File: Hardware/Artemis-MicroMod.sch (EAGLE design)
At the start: 24 parts, among them J2 MICROMOD-2222, U1 ARTEMIS_MODULESMD, U6 CH340E_MSOP10, Y1 32.768kHz

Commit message: Adding panel files for v10
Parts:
- removed J2: MICROMOD-2222, Teensy:MICROMOD-2222
- added C1: 0.1uF, SparkFun-Capacitors:0.1UF-0402T-16V-10%
- added J1: MICROMOD-2222, SparkFun-MicroMod:MICROMOD-2222
- added R2, R3, R6: 100k, SparkFun-Resistors:100KOHM-0402T-1/16W-1%
- added R4, R5, R7: 150k, SparkFun-Resistors:150KOHM-0402T-1/16W-1%
- added U2: TSV524, OpAmp:TSV524
- C17: device SparkFun-Capacitors:10NF-0603-50V-10% -> SparkFun-Capacitors:10NF-0402T-25V-10%
- C18: device SparkFun-Capacitors:0.1UF-0603-25V-(+80/-20%) -> SparkFun-Capacitors:0.1UF-0402T-16V-10%
- C20, C21: device SparkFun-Capacitors:0.1UF-0603-25V-5% -> SparkFun-Capacitors:0.1UF-0402T-16V-10%
- C28: value 1nF -> 1.0nF; device SparkFun-Capacitors:1.0NF/1000PF-0603-50V-10% -> SparkFun-Capacitors:1.0NF/1000PF-0402_TIGHT-50V-10%
- R14: device SparkFun-Resistors:100KOHM-0603-1/10W-1% -> SparkFun-Resistors:100KOHM-0402T-1/16W-1%
- R15: value 220k -> 220KOHM-0402T-1/16W-1%; device SparkFun-Resistors:220KOHM-0603-1/10W-1% -> SparkFun-Resistors:220KOHM-0402T-1/16W-1%
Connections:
- removed net GPIO11: J2.G11, U1.~AD11(PDMDATA)
- removed net GPIO8: J2.G8, U1.(SLNCE/I2SWCLK)D3
- removed net N$8: C13.2, U1.XI, Y1.1
- removed net RTS0: J2.RTS1, U1.(MOSI1/TX1/PDMCLK)D10
- removed net RX0: J2.RX1, U1.(SDA2/MISO2/RX1)~D25
- removed net TX0: J2.TX1, U1.(TX1/32KHZ/SWO)~D24
- new net 3.3V_EN: J1.3.3V_EN, U1.(SLNCE/I2SWCLK)D3
- new net CAM_PCLK: J1.AUD_IN/CAM_PCLK, U1.~AD11(PDMDATA)
- new net N$10: R2.1, R4.2, U2G1.+IN
- new net N$3: R6.1, R7.2, U2G3.+IN
- new net N$4: U1.XI
- new net N$5: C13.2, Y1.1
- new net N$9: R3.1, R5.2, U2G2.+IN
- new net RTS1: J1.RTS1, U1.(MOSI1/TX1/PDMCLK)D10
- new net RX1: J1.RX1, U1.(SDA2/MISO2/RX1)~D25
- new net SCALED_ADC0: U1.~AD32(SCCIO), U2G2.-IN, U2G2.OUT
- new net SCALED_ADC1: U1.~AD35(TX1/I2SDAT/PDMCLK), U2G3.-IN, U2G3.OUT
- new net SCALED_BATT_VIN/3: U1.~AD31(SCCCLK), U2G1.-IN, U2G1.OUT
- new net TX1: J1.TX1, U1.(TX1/32KHZ/SWO)~D24
- net !RESET!: now also J1.!RESET!; no longer J2.!RESET!
- net 3.3V: now also C1.1, J1.3.3V, J1.RTC_3V, U2G5.V+; no longer J2.3.3V
- net ADC0: now also J1.A0, R3.2; no longer J2.A0, U1.~AD32(SCCIO)
- net ADC1: now also J1.A1, R6.2; no longer J2.A1, U1.~AD35(TX1/I2SDAT/PDMCLK)
- net ADC_D+: now also J1.G10/ADC_D+/CAM_VSYNC; no longer J2.G10/ADC_D+
- net ADC_D-: now also J1.G9/ADC_D-/CAM_HSYNC; no longer J2.G9/ADC_D-
- net BATT_VIN/3: now also J1.BATT_VIN/3, R2.2; no longer J2.BATT_VIN/3, U1.~AD31(SCCCLK)
- net BOOT: now also J1.!BOOT!; no longer J2.!BOOT!
- net CLKOUT: now also J1.AUD_OUT/CAM_MCLK; no longer J2.AUD_MCLK/CLKOUT
- net CTS1: now also J1.CTS1; no longer J2.CTS1
- net D0: now also J1.D0; no longer J2.D0
- net D1: now also J1.D1/CAM_TRIG; no longer J2.D1
- net GND: now also C1.2, J1.GND, R4.1, R5.1, R7.1, U2G5.V-; no longer J2.GND
- net GPIO0: now also J1.G0/BUS0; no longer J2.G0
- net GPIO1: now also J1.G1/BUS1; no longer J2.G1
- net GPIO2: now also J1.G2/BUS2; no longer J2.G2
- net GPIO3: now also J1.G3/BUS3; no longer J2.G3
- net GPIO4: now also J1.G4/BUS4; no longer J2.G4
- net GPIO5: now also J1.G5/BUS5; no longer J2.G5
- net GPIO6: now also J1.G6/BUS6; no longer J2.G6
- net GPIO7: now also J1.G7/BUS7; no longer J2.G7
- net I2C_!INT!: now also J1.I2C_!INT!; no longer J2.I2C_!INT!
- net PDM_CLK: now also J1.AUD_BCLK; no longer J2.AUD_CLK
- net PDM_DATA: now also J1.AUD_LRCLK; no longer J2.AUD_DATA
- net PWM0: now also J1.PWM0; no longer J2.PWM0
- net PWM1: now also J1.PWM1; no longer J2.PWM1
- net SCL: now also J1.I2C_SCL; no longer J2.I2C_SCL
- net SCL1: now also J1.I2C_SCL1; no longer J2.I2C_SCL1
- net SDA: now also J1.I2C_SDA; no longer J2.I2C_SDA
- net SDA1: now also J1.I2C_SDA1; no longer J2.I2C_SDA1
- net SDIO_DATA0: now also J1.SDIO_DATA0/MISO1; no longer J2.SDIO_DATA0/MISO1
- net SDIO_DATA1: now also J1.SDIO_DATA1; no longer J2.SDIO_DATA1
- net SDIO_DATA2: now also J1.SDIO_DATA2; no longer J2.SDIO_DATA2
- net SDIO_DATA3: now also J1.SDIO_DATA3; no longer J2.SDIO_DATA3
- net SPI_!CS!: now also J1.SPI_!CS!; no longer J2.SPI_!CS!
- net SPI_MISO: now also J1.SPI_MISO; no longer J2.SPI_MISO
- net SPI_MOSI: now also J1.SPI_MOSI/LED_DAT; no longer J2.LED_DAT/SPI_MOSI
- net SPI_MOSI1: now also J1.SDIO_CMD/MOSI1; no longer J2.SDIO_CMD/MOSI1
- net SPI_SCK: now also J1.SPI_SCK/LED_CLK; no longer J2.LED_CLK/SPI_SCK
- net SPI_SCK1: now also J1.SDIO_CLK/SCK1; no longer J2.SDIO_CLK/SCK1
- net SWDCK: now also J1.SWDCK; no longer J2.SWDCK
- net SWDIO: now also J1.SWDIO; no longer J2.SWDIO
- net USB_D+: now also J1.USB_D+; no longer J2.USB_D+
- net USB_D-: now also J1.USB_D-; no longer J2.USB_D-
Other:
- note added: "MicroMod Connector"

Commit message: Routed CAM_PCLK
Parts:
- removed LOGO2: SFE_LOGO_FLAME.1_INCH, SparkFun-Aesthetics:SFE_LOGO_FLAME.1_INCH
- C11, C13: device SparkFun-Capacitors:15PF-0603-50V-5% -> SparkFun-Capacitors:15PF-0402T-50V-5%
- R1: device SparkFun-Resistors:1KOHM-0603-1/10W-1% -> SparkFun-Resistors:1KOHM-0402T-1/16W-1%
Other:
- note added: "3.3V to 2V Scaling"
- moved on the sheet: C1, R2, R3, R4, R5, R6, R7, U2G1, U2G2, U2G3, U2G5

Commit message: Double buffered ADC.
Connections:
- net N$3 renamed ADC1_BUFF2
- net N$9 renamed ADC0_BUFF2
- removed net N$10: R2.1, R4.2, U2G1.+IN
- new net ADC0_BUFF1: R3.2, U2G1.-IN, U2G1.OUT
- new net ADC_BUFF1: R6.2, U2G4.-IN, U2G4.OUT
- net ADC0: now also U2G1.+IN; no longer R3.2
- net ADC1: now also U2G4.+IN; no longer R6.2
- net SCALED_BATT_VIN/3: now also R2.1, R4.2; no longer U2G1.-IN, U2G1.OUT
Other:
- moved on the sheet: C11, C13, J1, R6, R7, U1, U2G1, U2G3, Y1

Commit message: Add reverse diode to prevent RTC 3.3V from driving 3.3V bus. Add test sketches.
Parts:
- added D7: 1A/23V/620mV, SparkFun-DiscreteSemi:DIODE-SCHOTTKY-BAT20J
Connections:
- new net 3.3V_MAIN: D7.A, J1.3.3V
- net 3.3V: now also D7.C; no longer J1.3.3V

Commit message: Add MicroMod logo, double route MCLK.
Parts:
- added LOGO2: SFE_LOGO_FLAME.1_INCH, SparkFun-Aesthetics:SFE_LOGO_FLAME.1_INCH
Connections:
- removed net SDIO_DATA0: J1.SDIO_DATA0/MISO1, U1.(PDMCLK/SWO)~D22, U1.(SDA0/MISO0/I2SDAT)~D6
- removed net SDIO_DATA3: J1.SDIO_DATA3, U1.(I2SWCLK/CMPOUT)~D23
- new net SPI_!CS!1: J1.SPI_!CS!1, U1.(BLEIF_IRQ/SWO/I2SWCLK)D41
- new net SPI_MISO1: J1.SPI_MISO1, U1.(SDA3/MISO3/RX1)~D43
- net CLKOUT: now also J1.AUD_MCLK
- net SPI_!CS!: now also J1.SPI_!CS!/SDIO_DATA3, U1.(I2SWCLK/CMPOUT)~D23; no longer J1.SPI_!CS!, U1.(BLEIF_IRQ/SWO/I2SWCLK)D41
- net SPI_MISO: now also J1.SPI_MISO/SDIO_DATA0, U1.(PDMCLK/SWO)~D22, U1.(SDA0/MISO0/I2SDAT)~D6; no longer J1.SPI_MISO, U1.(SDA3/MISO3/RX1)~D43
- net SPI_MOSI: now also J1.SPI_MOSI/SDIO_CMD, U1.(MOSI0/CLKOUT)~D7; no longer J1.SPI_MOSI/LED_DAT, U1.(MOSI3/RX1)D38
- net SPI_MOSI1: now also J1.SPI_MOSI1, U1.(MOSI3/RX1)D38; no longer J1.SDIO_CMD/MOSI1, U1.(MOSI0/CLKOUT)~D7
- net SPI_SCK: now also J1.SPI_SCK/SDIO_CLK, U1.(SCL0/SCK0)~D5; no longer J1.SPI_SCK/LED_CLK, U1.(SCL3/SCK3/TX1)~D42
- net SPI_SCK1: now also J1.SPI_SCK1, U1.(SCL3/SCK3/TX1)~D42; no longer J1.SDIO_CLK/SCK1, U1.(SCL0/SCK0)~D5
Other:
- note added: "0.65uA Leakage 0.3V drop at 10mA"
- note added: "Artemis"
- note added: "N. Seidle"
- note added: "Status LED"
- note added: "Vin: 1.755 - 3.63V"
- note added: "v1.2"
- moved on the sheet: C1, C11, C13, C17, C18, C20, C21, C28, D2, D7, J1, R1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

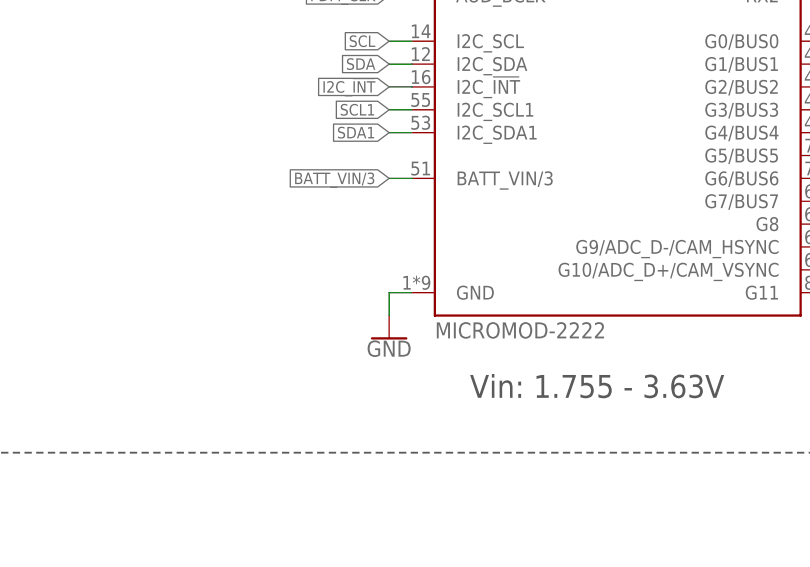
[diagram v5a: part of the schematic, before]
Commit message: Route from opamp for better AOI. fix DRC error. Add v1.2 panel files.
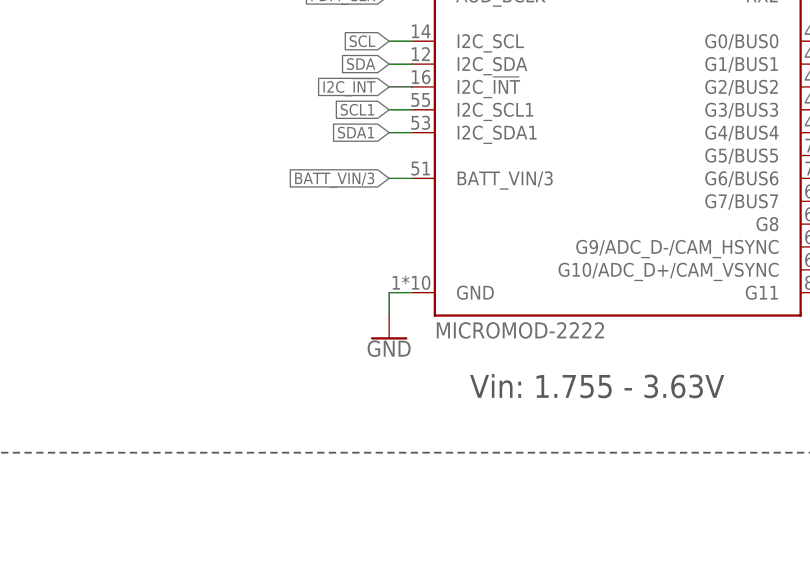
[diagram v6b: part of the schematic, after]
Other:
- moved on the sheet: J1
